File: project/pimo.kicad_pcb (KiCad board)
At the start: 2 copper layers, 65 x 56.5 mm, 8 parts, among them J1 RPi_GPIO, J11 Conn_01x03_Pin, U1 W25Q32JVSS

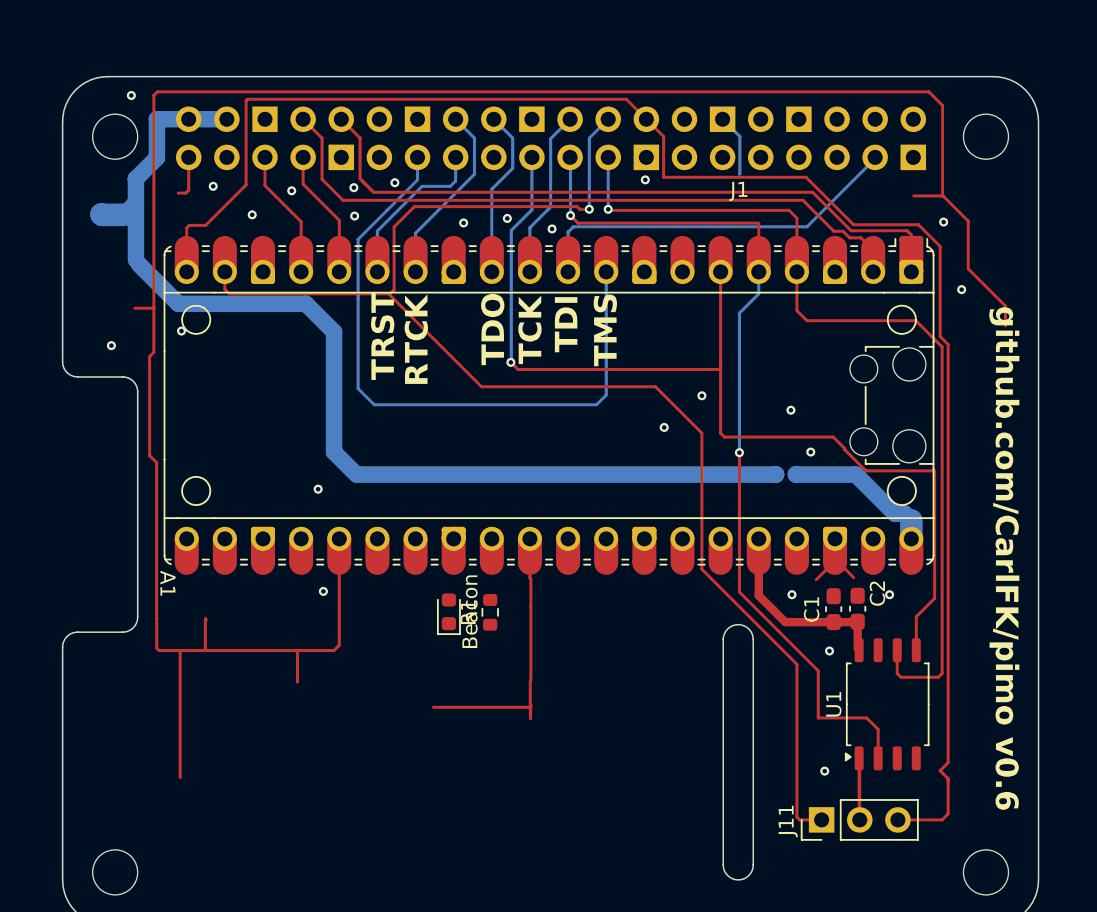
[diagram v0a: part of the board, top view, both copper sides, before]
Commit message: removed unused traces.  and some used ones.
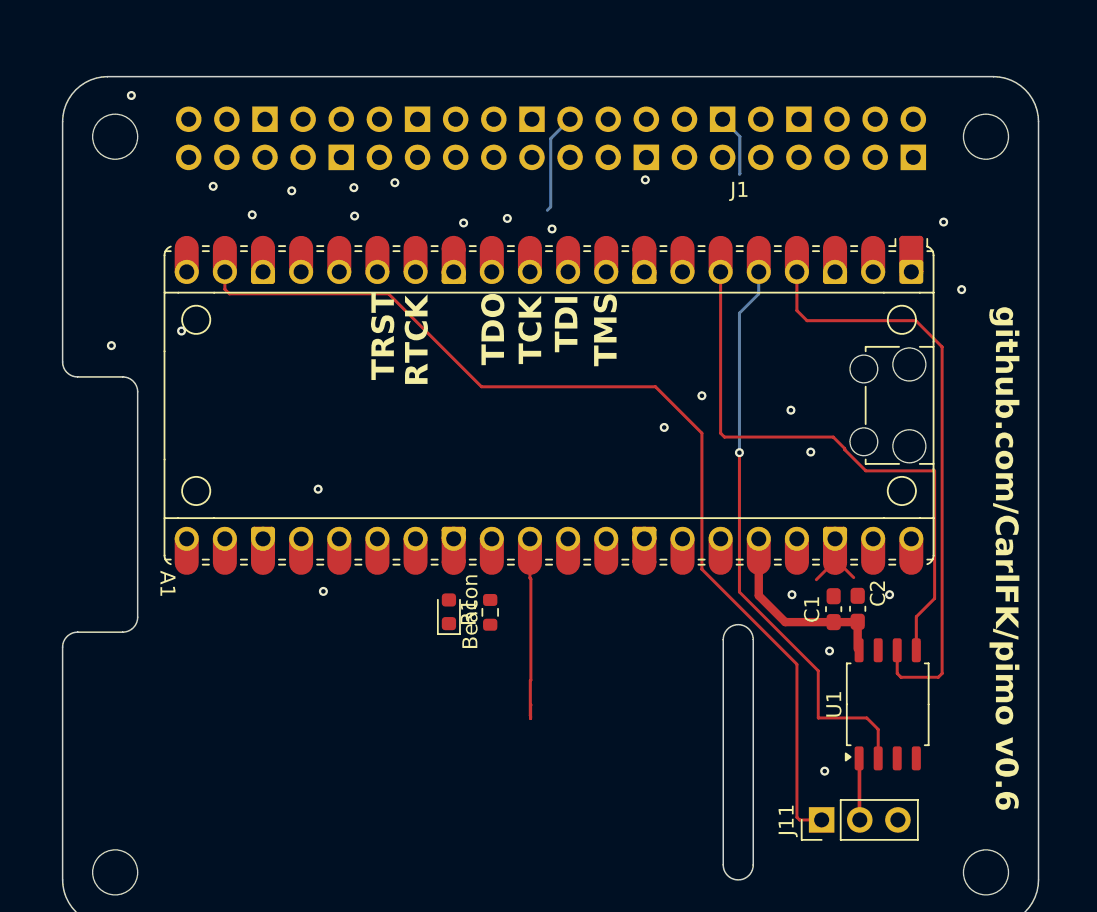
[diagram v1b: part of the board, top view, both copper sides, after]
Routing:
- net (no net): track 178.8 -> 0.00 mm
- net Net-(A1-GPIO19): track 142.1 -> 0.00 mm
- net /RPI_SPI_CE1: track 107.8 -> 0.00 mm
- net unconnected-(J1-BCM27-Pad13): track 42.5 -> 0.00 mm
- net /RPI_SPI_MOSI: track 67.7 -> 38.5 mm, vias 1 -> 0
- net unconnected-(J1-BCM26-Pad37): track 25.2 -> 0.00 mm
- net /RPI_SPI_CE0: track 91.7 -> 66.8 mm, vias 1 -> 0
- net /RPI_SPI_MISO: track 58.5 -> 38.7 mm, vias 2 -> 1
- net /RPI_SPI_CLK: track 59.6 -> 39.8 mm, vias 1 -> 0
- net /RTCK: track 12.3 -> 0.00 mm
- net unconnected-(J1-BCM24-Pad18): track 11.3 -> 0.00 mm
- net unconnected-(J1-BCM22-Pad15): track 10.9 -> 0.00 mm
- net unconnected-(A1-VBUS-Pad40): track 10.2 -> 0.00 mm
- net unconnected-(A1-RUN-Pad30): track 19.5 -> 13.0 mm
- net unconnected-(J1-BCM25-Pad22): track 11.5 -> 6.69 mm
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
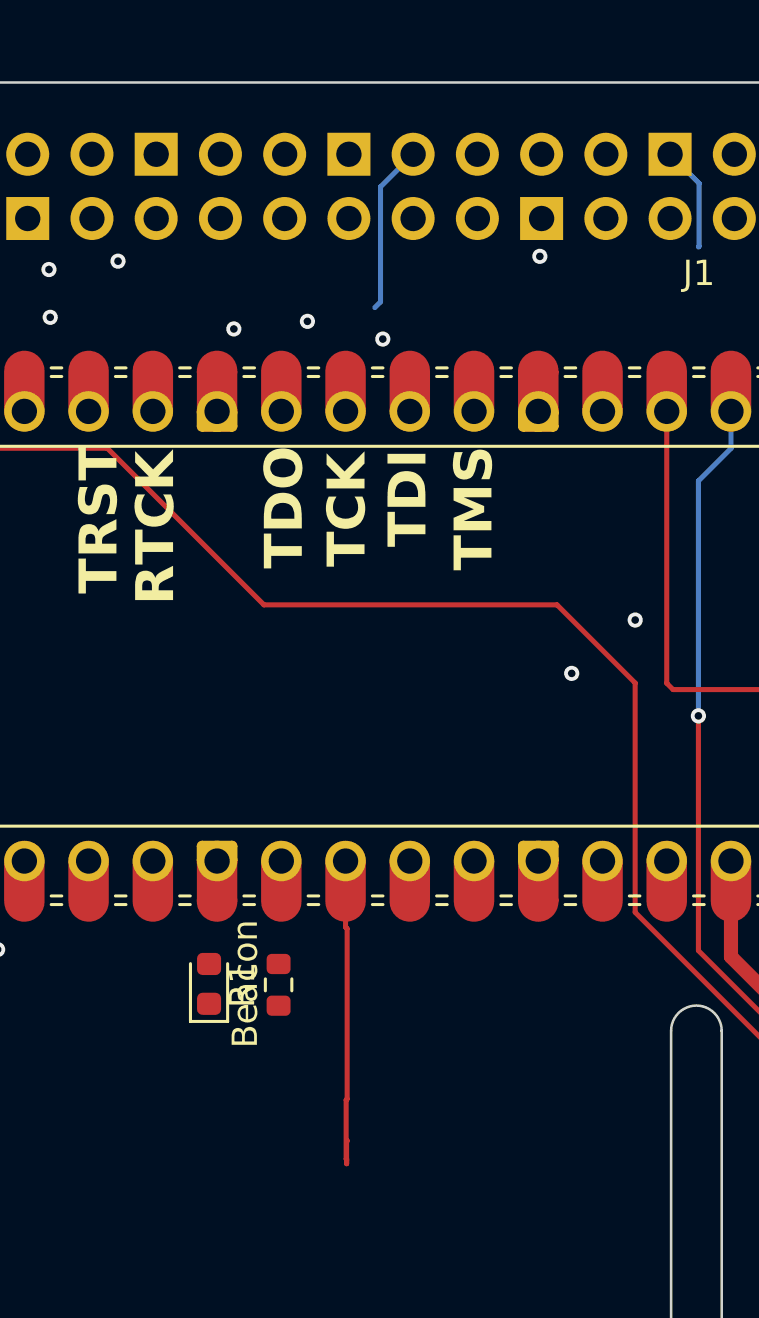
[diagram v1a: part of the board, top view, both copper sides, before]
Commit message: removed more unused traces.  and some used ones.
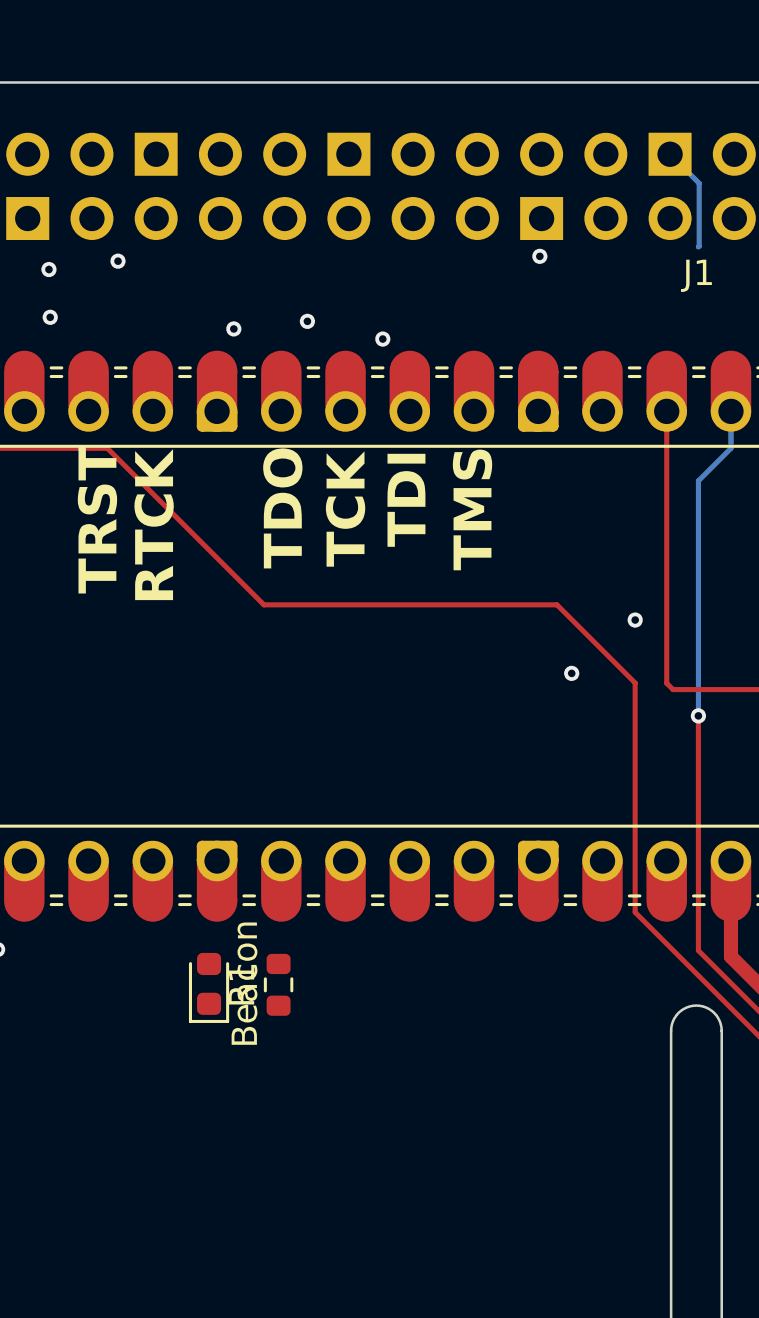
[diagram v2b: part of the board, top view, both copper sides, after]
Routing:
- net unconnected-(A1-RUN-Pad30): track 13.0 -> 0.00 mm
- net unconnected-(J1-BCM25-Pad22): track 6.69 -> 0.00 mm
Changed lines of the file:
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@@
-	)
-	(segment
-		(start 67.62 82.34)
-		(end 67.59 82.31)
-		(width 0.2)
-		(layer "F.Cu")
-		(net 3)
-	)
-	(segment
-		(start 67.5475 73.8925)
-		(end 67.61 73.955)
-		(width 0.2)
-		(layer "F.Cu")
-		(net 3)
-	)
-	(segment
-		(start 67.57 83.06)
-		(end 67.57 80.73)
-		(width 0.2)
-		(layer "F.Cu")
-		(net 3)
-	)
-	(segment
-		(start 67.61 80.69)
-		(end 67.57 80.73)
-		(width 0.2)
-		(layer "F.Cu")
-		(net 3)
-	)
-	(segment
-		(start 67.61 73.955)
-		(end 67.61 80.69)
-		(width 0.2)
-		(layer "F.Cu")
-		(net 3)
-	)
-	(segment
-		(start 67.59 83.25)
-		(end 67.59 83.08)
-		(width 0.2)
-		(layer "F.Cu")
-		(net 3)
-	)
-	(segment
-		(start 67.59 82.31)
-		(end 67.59 83.25)
-		(width 0.2)
-		(layer "F.Cu")
-		(net 3)
-	)
-	(segment
-		(start 67.5475 71.28)
-		(end 67.5475 73.8925)
-		(width 0.2)
-		(layer "F.Cu")
-		(net 3)
-	)
-	(segment
-		(start 67.59 83.08)
-		(end 67.57 83.06)
-		(width 0.2)
-		(layer "F.Cu")
-		(net 3)
 	)
 	(segment
@@
 		(net 55)
 	)
-	(segment
-		(start 68.93 49.17)
-		(end 68.93 44.623)
-		(width 0.2)
-		(layer "B.Cu")
-		(net 68)
-	)
-	(segment
-		(start 68.93 44.623)
-		(end 70.22 43.333)
-		(width 0.2)
-		(layer "B.Cu")
-		(net 68)
-	)
-	(segment
-		(start 68.705 49.395)
-		(end 68.93 49.17)
-		(width 0.2)
-		(layer "B.Cu")
-		(net 68)
-	)
 	(zone

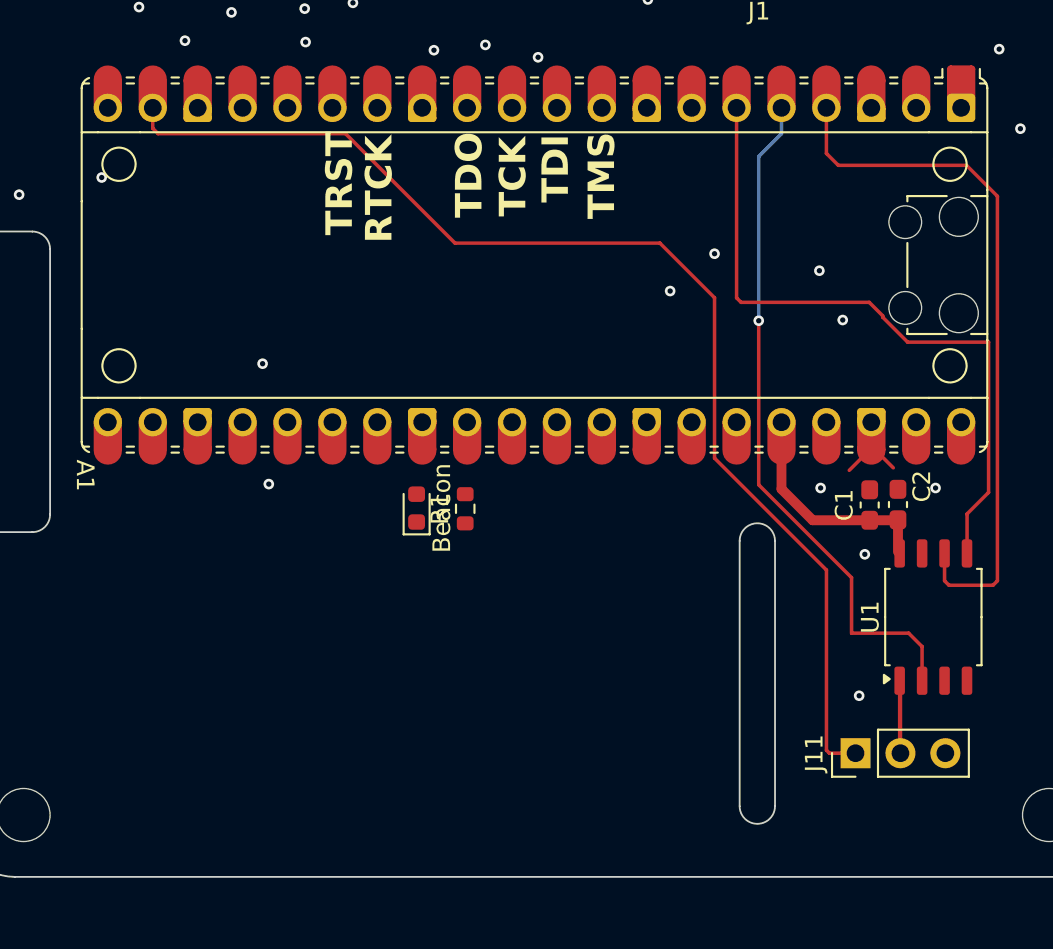
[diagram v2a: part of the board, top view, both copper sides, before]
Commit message: added back spi flasg CS trace.
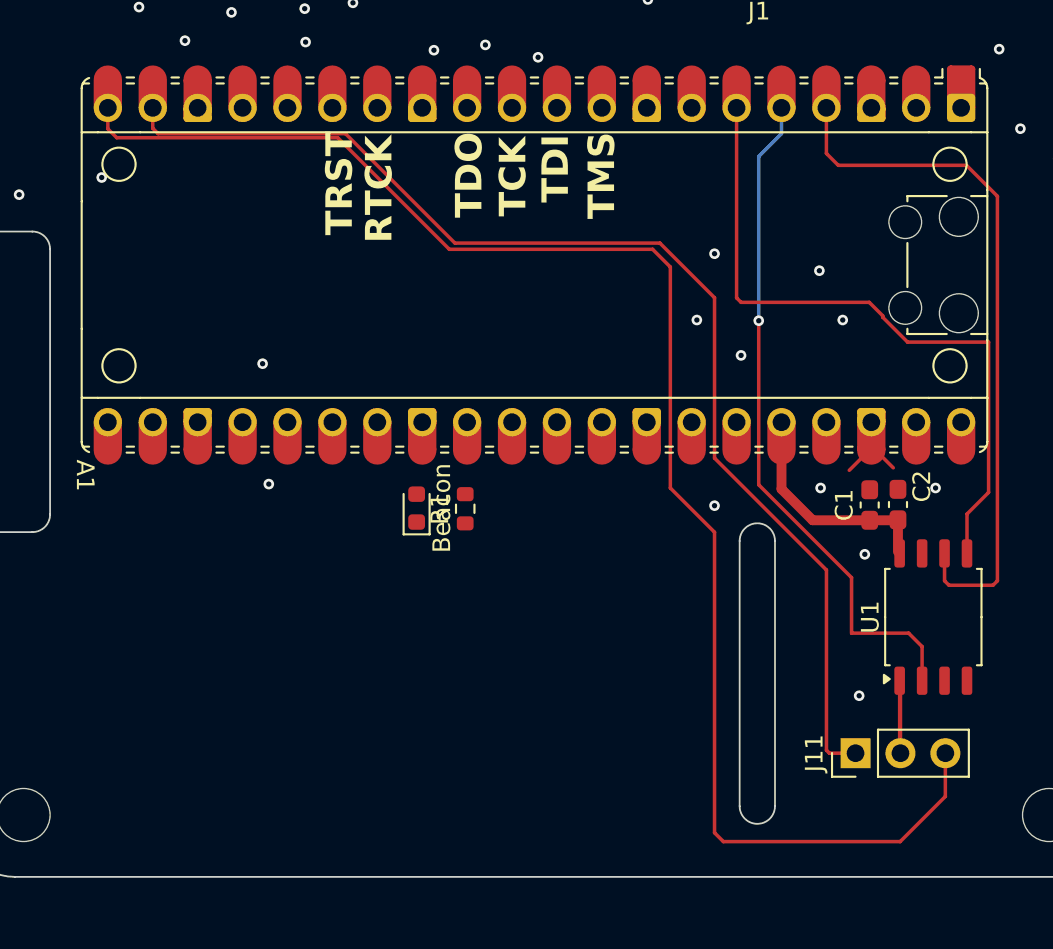
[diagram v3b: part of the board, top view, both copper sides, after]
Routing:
- net /RPI_SPI_CE1: track 0.00 -> 86.0 mm
- net GND: vias 25 -> 27
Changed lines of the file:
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@@
+	)
+	(via
+		(at 78 65.5)
+		(size 0.6)
+		(drill 0.3)
+		(layers "F.Cu" "B.Cu")
+		(free yes)
+		(net 7)
 	)
 	(via
@@
 	)
 	(via
-		(at 76.49 63.86)
-		(size 0.6)
-		(drill 0.3)
-		(layers "F.Cu" "B.Cu")
-		(free yes)
-		(net 7)
-	)
-	(via
 		(at 53.44 67.97)
 		(size 0.6)
@@
 	)
 	(via
+		(at 80.5 67.5)
+		(size 0.6)
+		(drill 0.3)
+		(layers "F.Cu" "B.Cu")
+		(free yes)
+		(net 7)
+	)
+	(via
 		(at 79 61.75)
 		(size 0.6)
@@
 	(via
 		(at 49.05 49.7)
+		(size 0.6)
+		(drill 0.3)
+		(layers "F.Cu" "B.Cu")
+		(free yes)
+		(net 7)
+	)
+	(via
+		(at 79 76)
 		(size 0.6)
 		(drill 0.3)
@@
 	)
 	(segment
+		(start 76.5 75)
+		(end 79 77.5)
+		(width 0.2)
+		(layer "F.Cu")
+		(net 10)
+	)
+	(segment
+		(start 79.5 95)
+		(end 89.5 95)
+		(width 0.2)
+		(layer "F.Cu")
+		(net 10)
+	)
+	(segment
+		(start 64 61.5)
+		(end 75.5 61.5)
+		(width 0.2)
+		(layer "F.Cu")
+		(net 10)
+	)
+	(segment
+		(start 44.6875 54.6875)
+		(end 45.189 55.189)
+		(width 0.2)
+		(layer "F.Cu")
+		(net 10)
+	)
+	(segment
+		(start 75.5 61.5)
+		(end 76.5 62.5)
+		(width 0.2)
+		(layer "F.Cu")
+		(net 10)
+	)
+	(segment
+		(start 79 77.5)
+		(end 79 94.5)
+		(width 0.2)
+		(layer "F.Cu")
+		(net 10)
+	)
+	(segment
+		(start 57.689 55.189)
+		(end 64 61.5)
+		(width 0.2)
+		(layer "F.Cu")
+		(net 10)
+	)
+	(segment
+		(start 44.6875 53.5)
+		(end 44.6875 54.6875)
+		(width 0.2)
+		(layer "F.Cu")
+		(net 10)
+	)
+	(segment
+		(start 92.055 92.445)
+		(end 92.055 90)
+		(width 0.2)
+		(layer "F.Cu")
+		(net 10)
+	)
+	(segment
+		(start 79 94.5)
+		(end 79.5 95)
+		(width 0.2)
+		(layer "F.Cu")
+		(net 10)
+	)
+	(segment
+		(start 45.189 55.189)
+		(end 57.689 55.189)
+		(width 0.2)
+		(layer "F.Cu")
+		(net 10)
+	)
+	(segment
+		(start 89.5 95)
+		(end 92.055 92.445)
+		(width 0.2)
+		(layer "F.Cu")
+		(net 10)
+	)
+	(segment
+		(start 76.5 62.5)
+		(end 76.5 75)
+		(width 0.2)
+		(layer "F.Cu")
+		(net 10)
+	)
+	(segment

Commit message: added most of the things.
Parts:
- added J2: Conn_01x05_Pin, Connector_PinHeader_2.54mm:PinHeader_1x05_P2.54mm_Vertical, F.Cu at (54.8, 79.2)
- added J3: Conn_ARM_JTAG_SWD_10, Connector_PinHeader_1.27mm:PinHeader_2x05_P1.27mm_Vertical, F.Cu at (98.8, 53.7)
- added J4: Conn_01x01, Connector_PinHeader_1.27mm:PinHeader_1x01_P1.27mm_Vertical, F.Cu at (59.9, 48.9)
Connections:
- A1 pad 15: /RESET -> /~{RESET}
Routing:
- net /~{RESET}: track 0.00 -> 45.8 mm
- net /SWO/TDO: track 0.00 -> 37.3 mm
- net /SWCLK/TCK: track 0.00 -> 34.5 mm
- net /NC/TDI: track 0.00 -> 33.0 mm
- net /SWDIO/TMS: track 0.00 -> 29.6 mm
- net Net-(A1-GPIO16): track 0.00 -> 9.01 mm
- net Net-(A1-GPIO17): track 0.00 -> 9.00 mm
- net Net-(A1-GPIO18): track 0.00 -> 7.95 mm
- net Net-(A1-GPIO19): track 0.00 -> 7.95 mm
- net /RTCK: track 0.00 -> 4.57 mm
- net GND: track 7.68 -> 3.56 mm, vias 27 -> 25
- net /RPI_SPI_CE0: track 66.8 -> 68.0 mm
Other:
- board text added: "github.com/CarlFK/pimo v0.9"
- board text removed: "github.com/CarlFK/pimo v0.6"

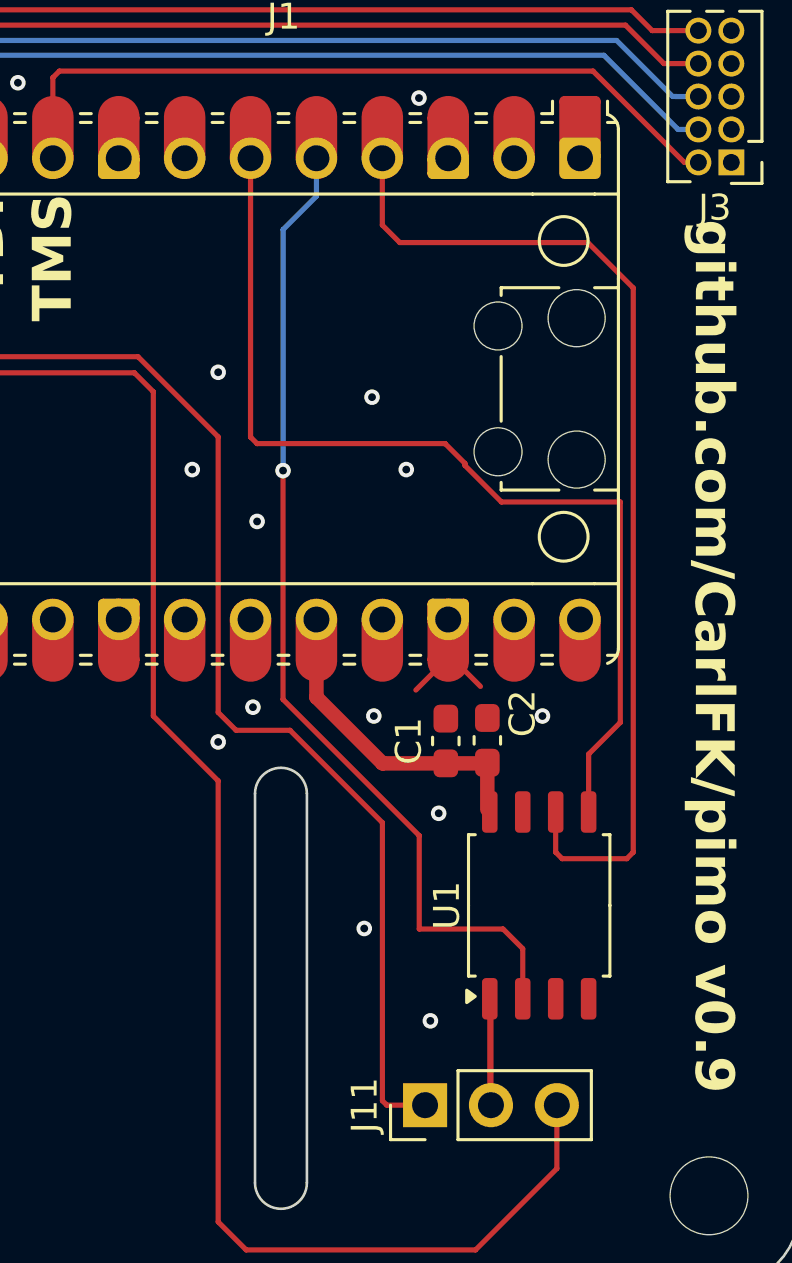
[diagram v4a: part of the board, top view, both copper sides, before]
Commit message: smaller spi footprint
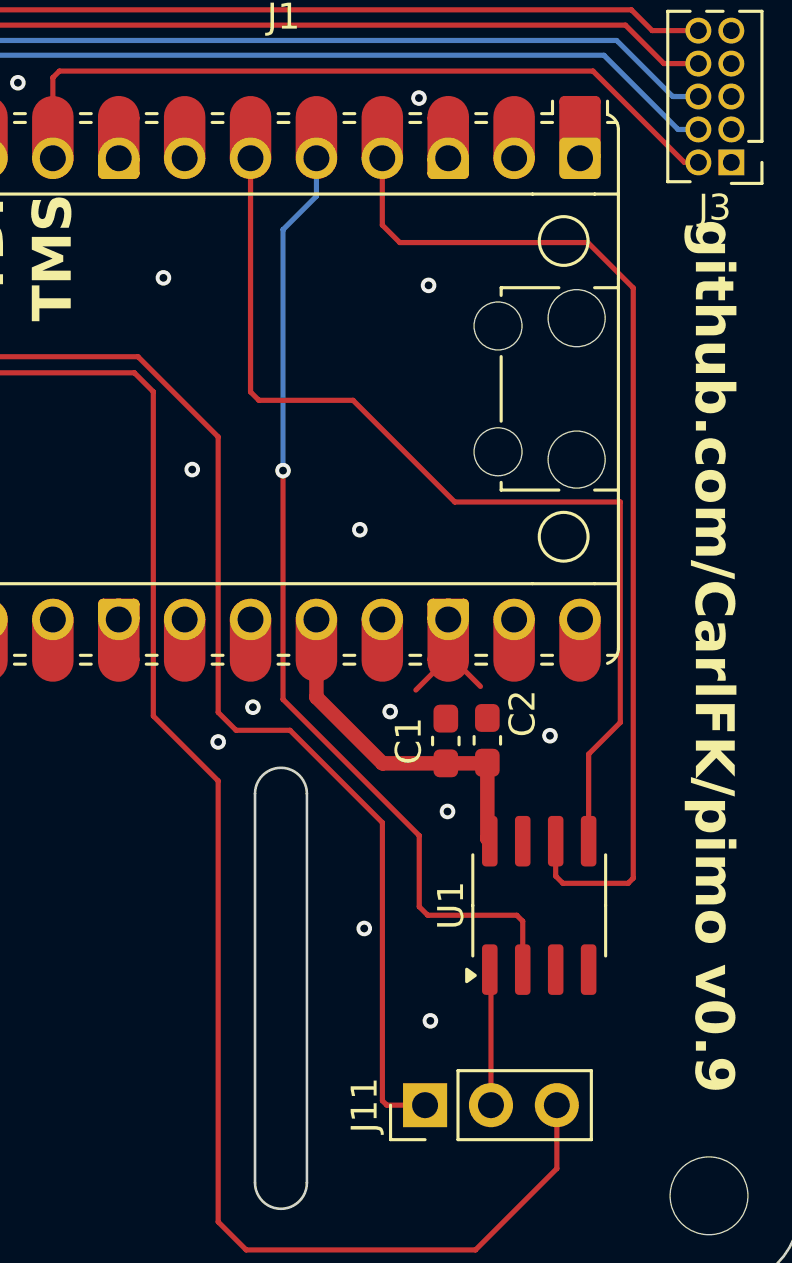
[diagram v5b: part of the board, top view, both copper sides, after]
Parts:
- U1: footprint Package_SO:SOIC-8_5.23x5.23mm_P1.27mm -> Package_SO:SOIC-8_3.9x4.9mm_P1.27mm
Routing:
- net Net-(J11-Pin_2): track 7.58 -> 5.24 mm
- net /pico3v3: track 12.4 -> 13.7 mm
- net /RPI_SPI_MISO: track 38.7 -> 37.6 mm
- net /RPI_SPI_CLK: track 39.8 -> 40.5 mm
- net GND: vias 25 -> 24
